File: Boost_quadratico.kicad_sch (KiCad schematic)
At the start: 29 parts

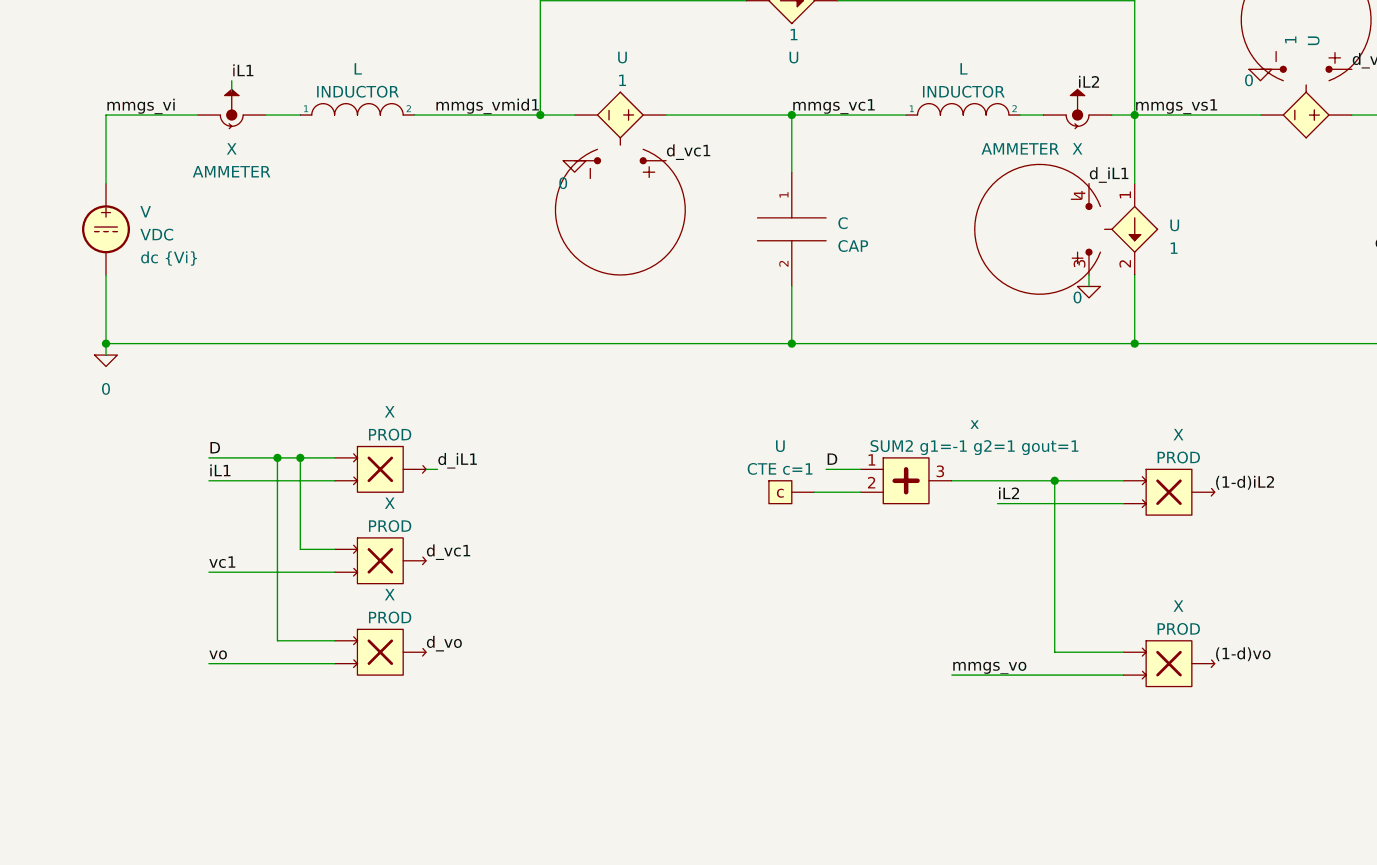
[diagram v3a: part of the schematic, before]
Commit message: Melhor resultado até agora, mas ainda oscilante
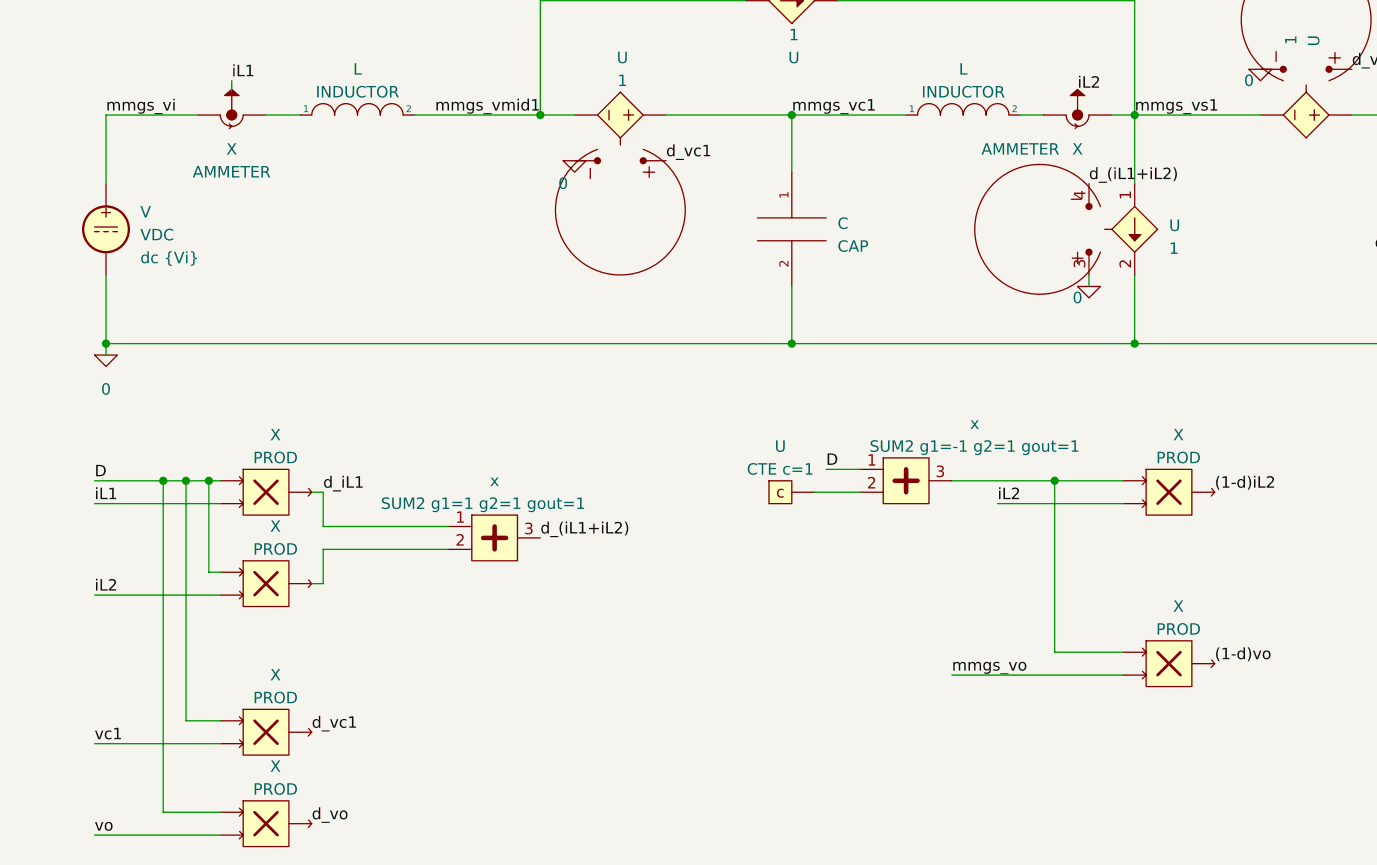
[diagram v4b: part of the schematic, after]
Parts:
- added X: product, symbol Signal Processing:product
- added x: sum2, symbol Signal Processing:sum2
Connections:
- net D: now also X.1
- net d_iL1: now also x.1; no longer U.4
- net iL2: now also X.2
- new net: X.3, x.2
- new net d_(iL1+iL2): U.4, x.3
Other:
- moved on the sheet: X

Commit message: Alterando a frequencia, quase encaixou.
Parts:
- added L: INDUCTOR, symbol pspice:INDUCTOR
- added X (x2): product, symbol Signal Processing:product
- added X: Voltmeter Compact, symbol Signal Processing:Voltmeter Compact
- added x: sum2, symbol Signal Processing:sum2
- S: Spice_Model ISWITCH reson=1m vgth=0.5 -> ISWITCH reson=1u vgth=0.5
- X: Spice_Model PWM3FIXED freq=10kHz -> PWM3FIXED freq=150kHz
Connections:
- net (1-d)iL2: now also U.3
- net (1-d)vo: now also U.3, x.1
- net 0: now also U.1, U.1, U.2, U.2, U.4; no longer U.2, U.3
- net d_(iL1+iL2): no longer U.4
- net d_iL1: no longer U.3
- net d_vc1: no longer U.3
- net d_vo: no longer U.3
- net iL1: now also X.2
- net mmgs_vc1: now also U.2, X.2, X.2; no longer U.1
- net mmgs_vmid1: now also U.1; no longer U.1, U.2
- net mmgs_vo: now also U.2, X.2; no longer U.1
- net mmgs_vs1: now also U.1; no longer U.1, U.2, U.2
- net vc1: no longer X.2
- net vmid1: now also L.1; no longer X.1
- net vo: no longer X.2
- net vs1: now also X.2
- net at X.1, X.1, x.3: now also X.1, X.1
- new net: L.2, X.1, X.1
- new net (1-d)(vc1-vo): x.3
- new net (1-d)iL1: U.3, X.3
- new net (1-d)vc1: U.3, X.3, x.2
- new net vd2: X.3
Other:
- note added: ".param Vi=48V ; Tensão de entrada .param L1=1000uH .param L2=100uH .param C1=1uF .param C2=10uF .param R=100 .param RSd=100u ; Resistência série nos diodos .param Vd=0 ; Queda de tensão nos diodos"
- note removed: ".param Vi=48V ; Tensão de entrada .param L1=1000uH .param L2=1000uH .param C1=1uF .param C2=100uF .param R=100 .param RSd=100u ; Resistência série nos diodos .param Vd=0 ; Queda de tensão nos diodos"
- moved on the sheet: U
